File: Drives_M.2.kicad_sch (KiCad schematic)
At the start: 93 parts, among them IC1 AP62800SJ-7, IC2 AP62800SJ-7, J13 Bus_M.2_Socket_M, M1 M.2 Solder Nut, M10 M.2 Screw, M11 M.2 Solder Nut, M12 M.2 Solder Nut, M13 M.2 Solder Nut, M14 M.2 Solder Nut, M15 M.2 Screw, M16 M.2 Solder Nut, M17 M.2 Solder Nut, M18 M.2 Solder Nut, M19 M.2 Solder Nut, M2 M.2 Solder Nut, M20 M.2 Screw, M3 M.2 Solder Nut, M4 M.2 Solder Nut, M5 M.2 Screw, M6 M.2 Solder Nut, M7 M.2 Solder Nut, M8 M.2 Solder Nut, M9 M.2 Solder Nut, U7 ASM1184, U8 ASEK-32.768KHZ-L-R-T, U9 TMP102xxDRL

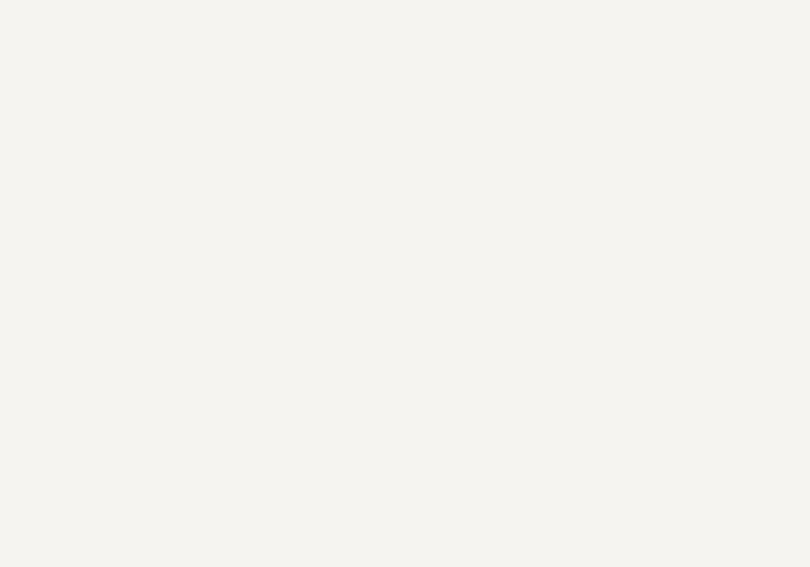
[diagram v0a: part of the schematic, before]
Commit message: Digital Reg with multiple v
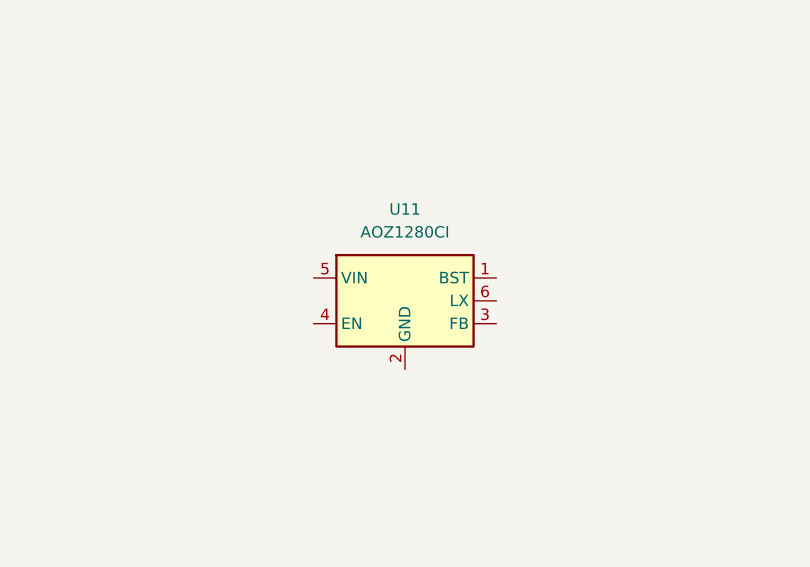
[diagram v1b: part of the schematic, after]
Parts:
- added U11: AOZ1280CI, Package_TO_SOT_SMD:SOT-23-6, symbol Regulator_Switching:AOZ1280CI
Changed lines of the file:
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@@
+	)
+	(symbol
+		(lib_id "Regulator_Switching:AOZ1280CI")
+		(at 254 203.2 0)
+		(unit 1)
+		(exclude_from_sim no)
+		(in_bom yes)
+		(on_board yes)
+		(dnp no)
+		(fields_autoplaced yes)
+		(property "Reference" "U11"
+			(at 254 193.04 0)
+			(effects
+				(font
+					(size 1.27 1.27)
+				)
+			)
+		)
+		(property "Value" "AOZ1280CI"
+			(at 254 195.58 0)
+			(effects
+				(font
+					(size 1.27 1.27)
+				)
+			)
+		)
+		(property "Footprint" "Package_TO_SOT_SMD:SOT-23-6"
+			(at 271.78 209.55 0)
+			(effects
+				(font
+					(size 1.27 1.27)
+				)
+				(hide yes)
+			)
+		)
+		(property "Datasheet" "http://aosmd.com/res/data_sheets/AOZ1280CI.pdf"
+			(at 247.65 209.55 0)
+			(effects
+				(font
+					(size 1.27 1.27)
+				)
+				(hide yes)
+			)
+		)
+		(property "Description" "1.2 A Simple Buck Regulator, 3-26V input, 1.5Mhz"
+			(at 254 203.2 0)
+			(effects
+				(font
+					(size 1.27 1.27)
+				)
+				(hide yes)
+			)
+		)
+		(pin "2"
+		)
+		(pin "5"
+		)
+		(pin "3"
+		)
+		(pin "4"
+		)
+		(pin "1"
+		)
+		(pin "6"
+		)
+		(instances
+			(project ""
+				(path "/0650c7a8-acba-429c-9f8e-eec0baf0bc1c/fede4c36-00cc-4d3d-b71c-5243ba232202/3838f96b-aabd-4e80-8b25-6301712882d2"
+					(reference "U11")
+					(unit 1)
+				)
+			)
+		)
 	)
 	(symbol

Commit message: Digital Reg Changed
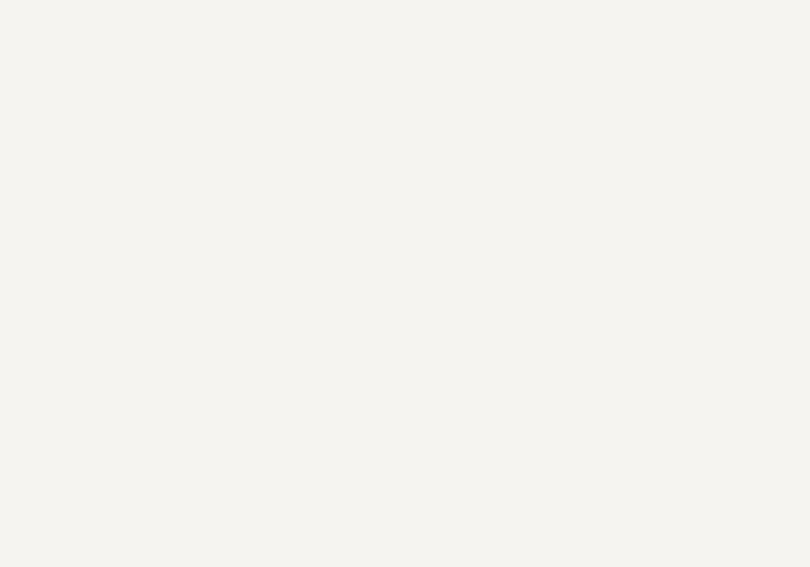
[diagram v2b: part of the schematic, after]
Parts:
- removed U11: AOZ1280CI, Package_TO_SOT_SMD:SOT-23-6, symbol Regulator_Switching:AOZ1280CI
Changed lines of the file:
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@@
-	)
-	(symbol
-		(lib_id "Regulator_Switching:AOZ1280CI")
-		(at 254 203.2 0)
-		(unit 1)
-		(exclude_from_sim no)
-		(in_bom yes)
-		(on_board yes)
-		(dnp no)
-		(fields_autoplaced yes)
-		(property "Reference" "U11"
-			(at 254 193.04 0)
-			(effects
-				(font
-					(size 1.27 1.27)
-				)
-			)
-		)
-		(property "Value" "AOZ1280CI"
-			(at 254 195.58 0)
-			(effects
-				(font
-					(size 1.27 1.27)
-				)
-			)
-		)
-		(property "Footprint" "Package_TO_SOT_SMD:SOT-23-6"
-			(at 271.78 209.55 0)
-			(effects
-				(font
-					(size 1.27 1.27)
-				)
-				(hide yes)
-			)
-		)
-		(property "Datasheet" "http://aosmd.com/res/data_sheets/AOZ1280CI.pdf"
-			(at 247.65 209.55 0)
-			(effects
-				(font
-					(size 1.27 1.27)
-				)
-				(hide yes)
-			)
-		)
-		(property "Description" "1.2 A Simple Buck Regulator, 3-26V input, 1.5Mhz"
-			(at 254 203.2 0)
-			(effects
-				(font
-					(size 1.27 1.27)
-				)
-				(hide yes)
-			)
-		)
-		(pin "2"
-		)
-		(pin "5"
-		)
-		(pin "3"
-		)
-		(pin "4"
-		)
-		(pin "1"
-		)
-		(pin "6"
-		)
-		(instances
-			(project ""
-				(path "/0650c7a8-acba-429c-9f8e-eec0baf0bc1c/fede4c36-00cc-4d3d-b71c-5243ba232202/3838f96b-aabd-4e80-8b25-6301712882d2"
-					(reference "U11")
-					(unit 1)
-				)
-			)
-		)
 	)
 	(symbol
